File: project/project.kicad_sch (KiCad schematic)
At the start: 11 parts, among them J1 Conn_01x02_Socket, SW1 SW_Push_45deg, SW2 SW_Push_45deg, SW3 SW_Push_45deg

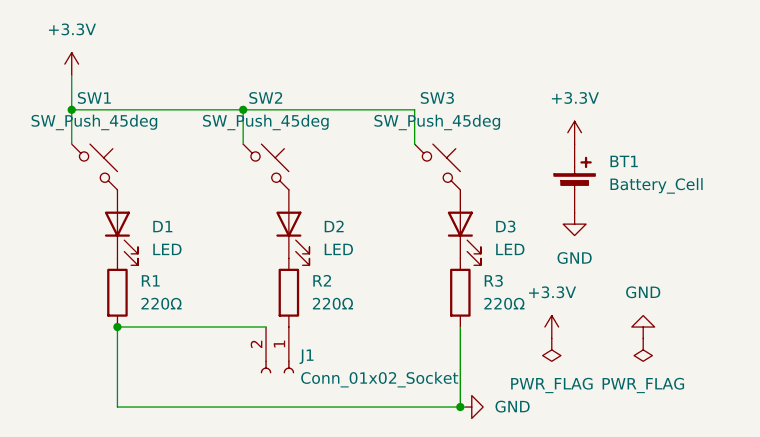
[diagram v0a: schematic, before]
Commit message: Put component in parallel
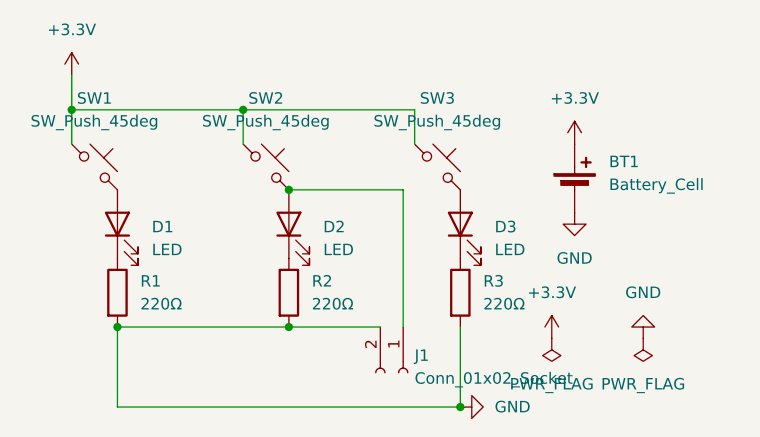
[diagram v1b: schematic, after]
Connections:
- net GND: now also R2.2
- net at J1.1 (Pin_1): now also D2.2 (A), SW2.2; no longer R2.2
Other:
- moved on the sheet: J1
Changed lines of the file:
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@@
+	)
+	(junction
+		(at 97.79 68.58)
+		(diameter 0)
+		(color 0 0 0 0)
+	)
+	(junction
+		(at 97.79 83.82)
+		(diameter 0)
+		(color 0 0 0 0)
 	)
 	(junction
@@
 	(wire
 		(pts
+			(xy 97.79 83.82) (xy 107.95 83.82)
+		)
+		(stroke
+			(width 0)
+			(type default)
+		)
+	)
+	(wire
+		(pts
 			(xy 73.66 59.69) (xy 92.71 59.69)
 		)
@@
 	(wire
 		(pts
-			(xy 78.74 83.82) (xy 95.25 83.82)
+			(xy 97.79 68.58) (xy 110.49 68.58)
 		)
 		(stroke
@@
 		(pts
 			(xy 73.66 59.69) (xy 73.66 63.5)
+		)
+		(stroke
+			(width 0)
+			(type default)
+		)
+	)
+	(wire
+		(pts
+			(xy 110.49 68.58) (xy 110.49 83.82)
+		)
+		(stroke
+			(width 0)
+			(type default)
+		)
+	)
+	(wire
+		(pts
+			(xy 78.74 83.82) (xy 97.79 83.82)
 		)
 		(stroke
@@
 	(symbol
 		(lib_id "Connector:Conn_01x02_Socket")
-		(at 97.79 88.9 270)
+		(at 110.49 88.9 270)
 		(unit 1)
 		(exclude_from_sim no)
@@
 		(fields_autoplaced yes)
 		(property "Reference" "J1"
-			(at 99.06 86.9949 90)
+			(at 111.76 86.9949 90)
 			(effects
 				(font
@@
 		)
 		(property "Value" "Conn_01x02_Socket"
-			(at 99.06 89.5349 90)
+			(at 111.76 89.5349 90)
 			(effects
 				(font
@@
 		)
 		(property "Footprint" "Connector_PinHeader_2.54mm:PinHeader_1x02_P2.54mm_Vertical"
-			(at 97.79 88.9 0)
+			(at 110.49 88.9 0)
 			(effects
 				(font
@@
 		)
 		(property "Datasheet" "~"
-			(at 97.79 88.9 0)
+			(at 110.49 88.9 0)
 			(effects
 				(font
@@
 		)
 		(property "Description" "Generic connector, single row, 01x02, script generated"
-			(at 97.79 88.9 0)
-			(effects
-				(font
+			(at 110.49 88.9 0)
+			(effects
+				(font
